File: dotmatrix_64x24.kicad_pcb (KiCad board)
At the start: 2 copper layers, 180 x 100 mm, 788 parts, among them CON1 BARREL_JACK, P1 CONN_01X09, P2 CONN_01X09, P3 CONN_01X04, P4 CONN_01X03, P5 USB_OTG, P6 CONN_01X03, Q1 NJL7302L-F3, Q3 Q_NPN_BCE RN5006, SW1 SW_PUSH_SMALL_H, SW2 SW_PUSH_SMALL_H, SW3 SW_PUSH_SMALL_H, SW4 SW_PUSH_SMALL_H, SW5 SW_PUSH_SMALL_H, SW6 SW_PUSH_SMALL_H, SW7 SW_PUSH_SMALL_H, SW8 SW_PUSH_SMALL_H, U1 WROOM-02, U10 LED1642GW, U11 LED1642GW, U12 AE-BME280, U13 TPS54426, U14 NJU7223, U15 DS1307, U16 CH340G, U17 OSRB38C9AA, U18 BME280, U2 74HC595-alt-vdd, U3 TD62783, U4 74HC595-alt-vdd, U5 TD62783, U6 LED1642GW, U7 74HC595-alt-vdd, U8 TD62783, U9 LED1642GW, X1 CRYSTAL_SMD, Y1 12MHz

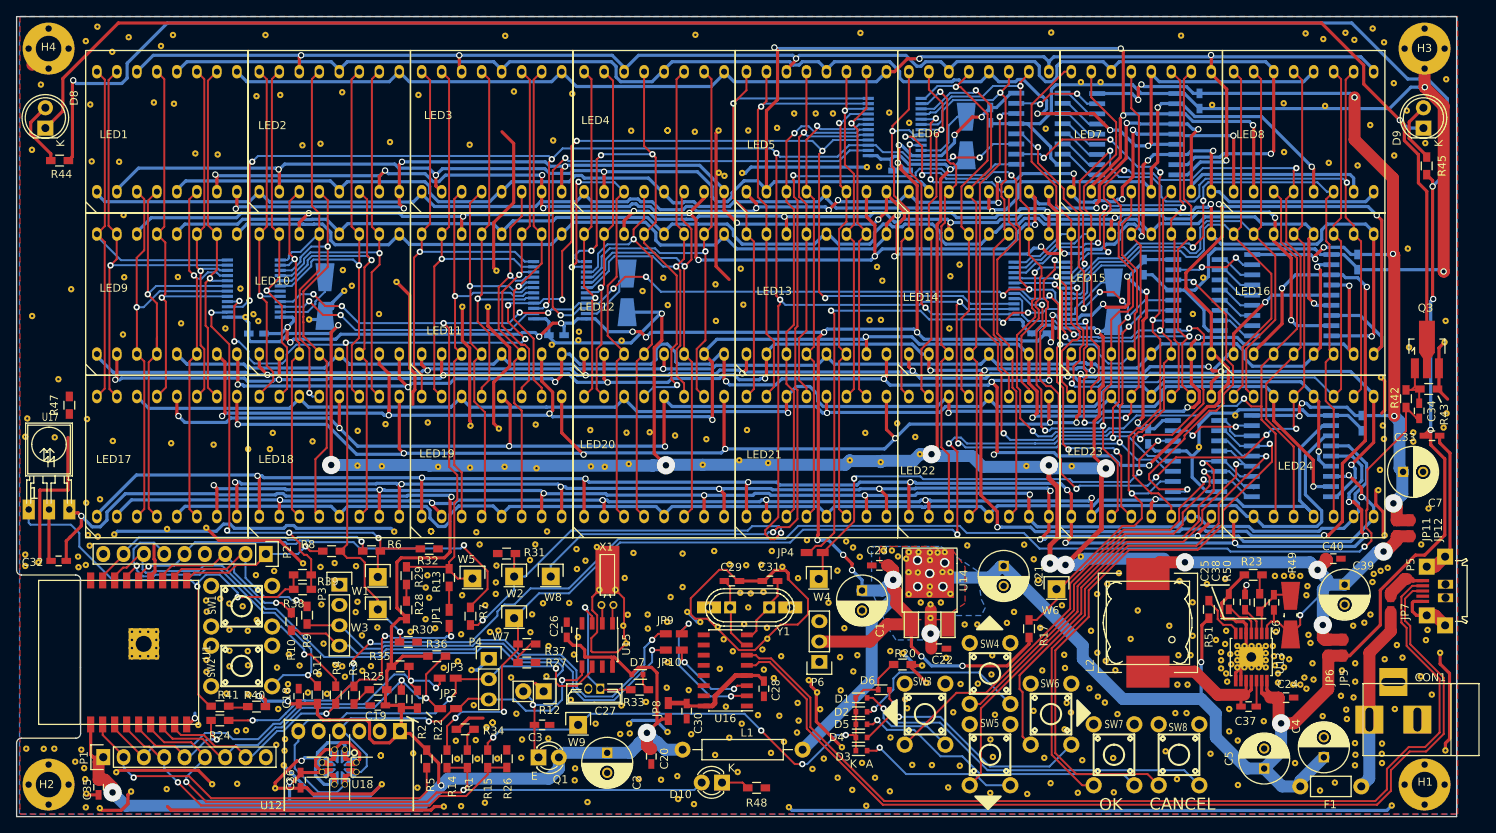
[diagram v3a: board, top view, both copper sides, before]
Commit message: Trace fixes
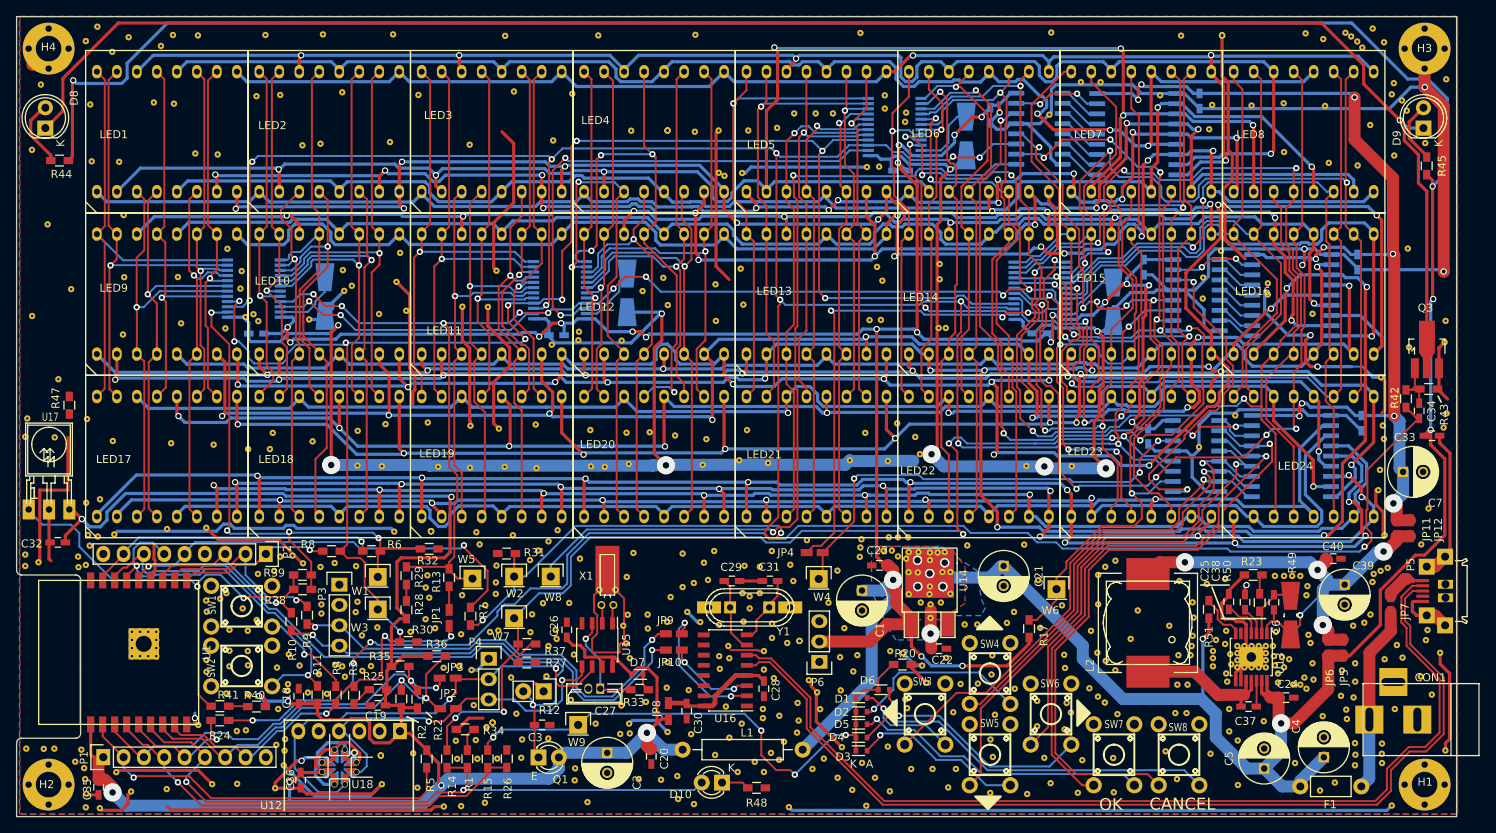
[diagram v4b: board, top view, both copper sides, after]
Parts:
- removed the REF** at (105.8, 88.4)
- removed the REF** at (99.6, 88.3)
- removed the REF** at (107.7, 80.8)
- removed the REF** at (101.1, 80.5)
- removed the REF** at (109.7, 82.2)
- removed the REF** at (139.1, 79.8)
- removed the REF** at (82.2, 89.6)
- removed the REF** at (103.5, 85.9)
- removed the REF** at (105.8, 89.8)
- removed the REF** at (105.1, 80.5)
- removed the REF** at (50.4, 90.4)
- removed the REF** at (159.0, 49.2)
- removed the REF** at (120.0, 67.7)
- removed the REF** at (83.1, 80.0)
- removed the REF** at (84.5, 78.3)
- removed the REF** at (82.0, 81.1)
- removed the REF** at (121.2, 102.1)
- removed the REF** at (186.6, 64.0)
- removed the REF** at (186.6, 65.1)
- removed the REF** at (140.6, 26.0)
- removed the REF** at (102.9, 87.9)
- removed the REF** at (105.2, 91.1)
- removed the REF** at (101.5, 91.3)
- removed the REF** at (103.2, 80.6)
- removed the REF** at (103.8, 84.1)
- removed the REF** at (102.5, 84.0)
- removed the REF** at (105.4, 83.9)
- removed the REF** at (100.4, 89.8)
- removed the REF** at (82.0, 78.6)
- removed the REF** at (67.2, 92.6)
- removed the REF** at (145.0, 79.5)
- added REF**: stitch-via-0.6mm, components:stitch-via-0.8mm, F.Cu at (161.1, 26.1)
- added REF**: stitch-via-0.6mm, components:stitch-via-0.8mm, F.Cu at (179.6, 15.1)
- added REF**: stitch-via-0.6mm, components:stitch-via-0.8mm, F.Cu at (185.2, 22.5)
- added REF**: stitch-via-0.6mm, components:stitch-via-0.8mm, F.Cu at (183.9, 21.7)
- added REF** (x2): stitch-via-0.6mm, components:stitch-via-0.8mm, F.Cu at (109.9, 90.0)
- added REF**: stitch-via-0.6mm, components:stitch-via-0.8mm, F.Cu at (59.9, 41.5)
- added REF**: stitch-via-0.6mm, components:stitch-via-0.8mm, F.Cu at (60.7, 48.8)
- added REF**: stitch-via-0.6mm, components:stitch-via-0.8mm, F.Cu at (38.4, 41.0)
- added REF**: stitch-via-0.6mm, components:stitch-via-0.8mm, F.Cu at (40.1, 43.8)
- added REF**: stitch-via-0.6mm, components:stitch-via-0.8mm, F.Cu at (123.2, 24.0)
- added REF**: stitch-via-0.6mm, components:stitch-via-0.8mm, F.Cu at (141.1, 24.3)
- added REF**: stitch-via-0.6mm, components:stitch-via-0.8mm, F.Cu at (120.5, 21.8)
- added REF**: stitch-via-0.6mm, components:stitch-via-0.8mm, F.Cu at (127.3, 50.9)
- added REF**: stitch-via-0.6mm, components:stitch-via-0.8mm, F.Cu at (174.0, 49.1)
- added REF**: stitch-via-0.6mm, components:stitch-via-0.8mm, F.Cu at (168.4, 46.7)
- added REF**: stitch-via-0.6mm, components:stitch-via-0.8mm, F.Cu at (168.4, 45.3)
- added REF**: stitch-via-0.6mm, components:stitch-via-0.8mm, F.Cu at (160.3, 47.2)
- added REF**: stitch-via-0.6mm, components:stitch-via-0.8mm, F.Cu at (162.6, 41.3)
- added REF** (x2): stitch-via-0.6mm, components:stitch-via-0.8mm, F.Cu at (162.7, 14.4)
- added REF**: stitch-via-0.6mm, components:stitch-via-0.8mm, F.Cu at (154.9, 21.8)
- added REF**: stitch-via-0.6mm, components:stitch-via-0.8mm, F.Cu at (166.4, 23.1)
- added REF**: stitch-via-0.6mm, components:stitch-via-0.8mm, F.Cu at (103.6, 84.5)
- added REF**: stitch-via-0.6mm, components:stitch-via-0.8mm, F.Cu at (102.9, 87.6)
- added REF**: stitch-via-0.6mm, components:stitch-via-0.8mm, F.Cu at (108.7, 80.5)
- added REF**: stitch-via-0.6mm, components:stitch-via-0.8mm, F.Cu at (97.9, 80.3)
- added REF**: stitch-via-0.6mm, components:stitch-via-0.8mm, F.Cu at (96.6, 82.8)
- added REF**: stitch-via-0.6mm, components:stitch-via-0.8mm, F.Cu at (99.8, 91.9)
- added REF**: stitch-via-0.6mm, components:stitch-via-0.8mm, F.Cu at (108.3, 90.3)
- added REF**: stitch-via-0.6mm, components:stitch-via-0.8mm, F.Cu at (98.4, 82.4)
- added REF**: stitch-via-0.6mm, components:stitch-via-0.8mm, F.Cu at (109.1, 82.5)
- added REF**: stitch-via-0.6mm, components:stitch-via-0.8mm, F.Cu at (103.0, 80.6)
- added REF**: stitch-via-0.6mm, components:stitch-via-0.8mm, F.Cu at (15.9, 38.0)
- added REF**: stitch-via-0.6mm, components:stitch-via-0.8mm, F.Cu at (104.9, 80.8)
- added REF**: stitch-via-0.6mm, components:stitch-via-0.8mm, F.Cu at (104.9, 84.1)
- added REF**: stitch-via-0.6mm, components:stitch-via-0.8mm, F.Cu at (105.3, 99.7)
- added REF**: stitch-via-0.6mm, components:stitch-via-0.8mm, F.Cu at (101.1, 92.2)
- added REF**: stitch-via-0.6mm, components:stitch-via-0.8mm, F.Cu at (101.0, 90.7)
- added REF**: stitch-via-0.6mm, components:stitch-via-0.8mm, F.Cu at (106.4, 89.7)
- added REF**: stitch-via-0.6mm, components:stitch-via-0.8mm, F.Cu at (106.4, 87.9)
- added REF**: stitch-via-0.6mm, components:stitch-via-0.8mm, F.Cu at (102.7, 84.1)
- added REF**: stitch-via-0.6mm, components:stitch-via-0.8mm, F.Cu at (103.6, 86.0)
- added REF**: stitch-via-0.6mm, components:stitch-via-0.8mm, F.Cu at (99.8, 88.0)
- added REF**: stitch-via-0.6mm, components:stitch-via-0.8mm, F.Cu at (34.7, 14.4)
- added REF**: stitch-via-0.6mm, components:stitch-via-0.8mm, F.Cu at (159.1, 87.1)
- added REF**: stitch-via-0.6mm, components:stitch-via-0.8mm, F.Cu at (158.9, 90.7)
- added REF**: stitch-via-0.6mm, components:stitch-via-0.8mm, F.Cu at (139.6, 97.5)
- added REF**: stitch-via-0.6mm, components:stitch-via-0.8mm, F.Cu at (147.2, 85.5)
- added REF**: stitch-via-0.6mm, components:stitch-via-0.8mm, F.Cu at (120.9, 103.3)
- added REF**: stitch-via-0.6mm, components:stitch-via-0.8mm, F.Cu at (120.9, 67.6)
- added REF**: stitch-via-0.6mm, components:stitch-via-0.8mm, F.Cu at (123.4, 77.1)
- added REF**: stitch-via-0.6mm, components:stitch-via-0.8mm, F.Cu at (122.2, 77.1)
- added REF**: stitch-via-0.6mm, components:stitch-via-0.8mm, F.Cu at (121.0, 77.1)
- added REF**: stitch-via-0.6mm, components:stitch-via-0.8mm, F.Cu at (105.4, 106.4)
- added REF**: stitch-via-0.6mm, components:stitch-via-0.8mm, F.Cu at (50.3, 14.2)
- added REF**: stitch-via-0.6mm, components:stitch-via-0.8mm, F.Cu at (104.3, 105.2)
- added REF**: stitch-via-0.6mm, components:stitch-via-0.8mm, F.Cu at (107.3, 104.9)
- added REF**: stitch-via-0.6mm, components:stitch-via-0.8mm, F.Cu at (46.5, 79.4)
- added REF**: stitch-via-0.6mm, components:stitch-via-0.8mm, F.Cu at (45.0, 79.5)
- added REF**: stitch-via-0.6mm, components:stitch-via-0.8mm, F.Cu at (82.4, 79.8)
- added REF**: stitch-via-0.6mm, components:stitch-via-0.8mm, F.Cu at (67.3, 93.2)
- added REF**: stitch-via-0.6mm, components:stitch-via-0.8mm, F.Cu at (74.0, 76.8)
- added REF**: stitch-via-0.6mm, components:stitch-via-0.8mm, F.Cu at (77.2, 78.7)
- added REF**: stitch-via-0.6mm, components:stitch-via-0.8mm, F.Cu at (88.6, 92.2)
- added REF**: stitch-via-0.6mm, components:stitch-via-0.8mm, F.Cu at (79.5, 89.8)
- added REF**: stitch-via-0.6mm, components:stitch-via-0.8mm, F.Cu at (59.1, 14.2)
- added REF**: stitch-via-0.6mm, components:stitch-via-0.8mm, F.Cu at (79.4, 88.6)
- added REF**: stitch-via-0.6mm, components:stitch-via-0.8mm, F.Cu at (50.1, 86.6)
- added REF**: stitch-via-0.6mm, components:stitch-via-0.8mm, F.Cu at (84.7, 14.4)
- added REF**: stitch-via-0.6mm, components:stitch-via-0.8mm, F.Cu at (180.2, 15.9)
- moved REF** 4.12 mm to (136.8, 96.0)
- moved REF** 2.49 mm to (127.4, 42.9)
- moved REF** 2.39 mm to (147.2, 81.8)
- moved C32 2.31 mm to (17.1, 77.7)
- moved REF** 2.25 mm to (105.4, 91.3)
- moved REF** 2.17 mm to (148.1, 80.8)
- moved REF** 1.98 mm to (139.6, 100.7)
- moved REF** 1.92 mm to (117.6, 77.3)
- moved REF** 1.69 mm to (78.5, 77.6)
- moved REF** 1.61 mm to (149.4, 80.0)
- moved REF** 1.40 mm to (127.4, 44.8)
- moved REF** 1.34 mm to (38.2, 84.1)
- moved REF** 1.33 mm to (79.6, 76.2)
- moved REF** 1.05 mm to (161.5, 92.2)
- moved REF** 1.05 mm to (161.5, 93.2)
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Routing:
- net GND: track 1068.8 -> 1059.9 mm, vias 16 -> 19
- net /LEDLOGICVDD: track 313.1 -> 306.8 mm, vias 24 -> 21
- net /ESPVDD: track 289.0 -> 283.2 mm
- net /Sheet57A04605/HC595LATCH: track 183.5 -> 188.7 mm, vias 10 -> 11
- net Net-(C27-Pad1): track 17.2 -> 13.1 mm
- net /Sheet57A04605/r2: track 181.9 -> 185.4 mm
- net /Sheet57A04605/BUTTONSENSE: track 66.6 -> 69.4 mm
- net /IR_OUT: track 178.7 -> 180.8 mm
- net /Sheet57A04605/r9: track 182.0 -> 184.0 mm
- net /Sheet57A04605/HC595SER: track 59.8 -> 57.9 mm
- net Net-(D3-Pad2): track 20.0 -> 21.7 mm
- net /Sheet57A04605/SEL6: track 76.8 -> 78.3 mm
- net /Sheet57A04605/SEL5: track 66.9 -> 68.4 mm
- net /Sheet57A04605/SEL1: track 61.1 -> 62.6 mm
- net /Sheet57A04605/SEL2: track 53.2 -> 54.3 mm
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
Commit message: Improved crystal stability by adding local ground plane
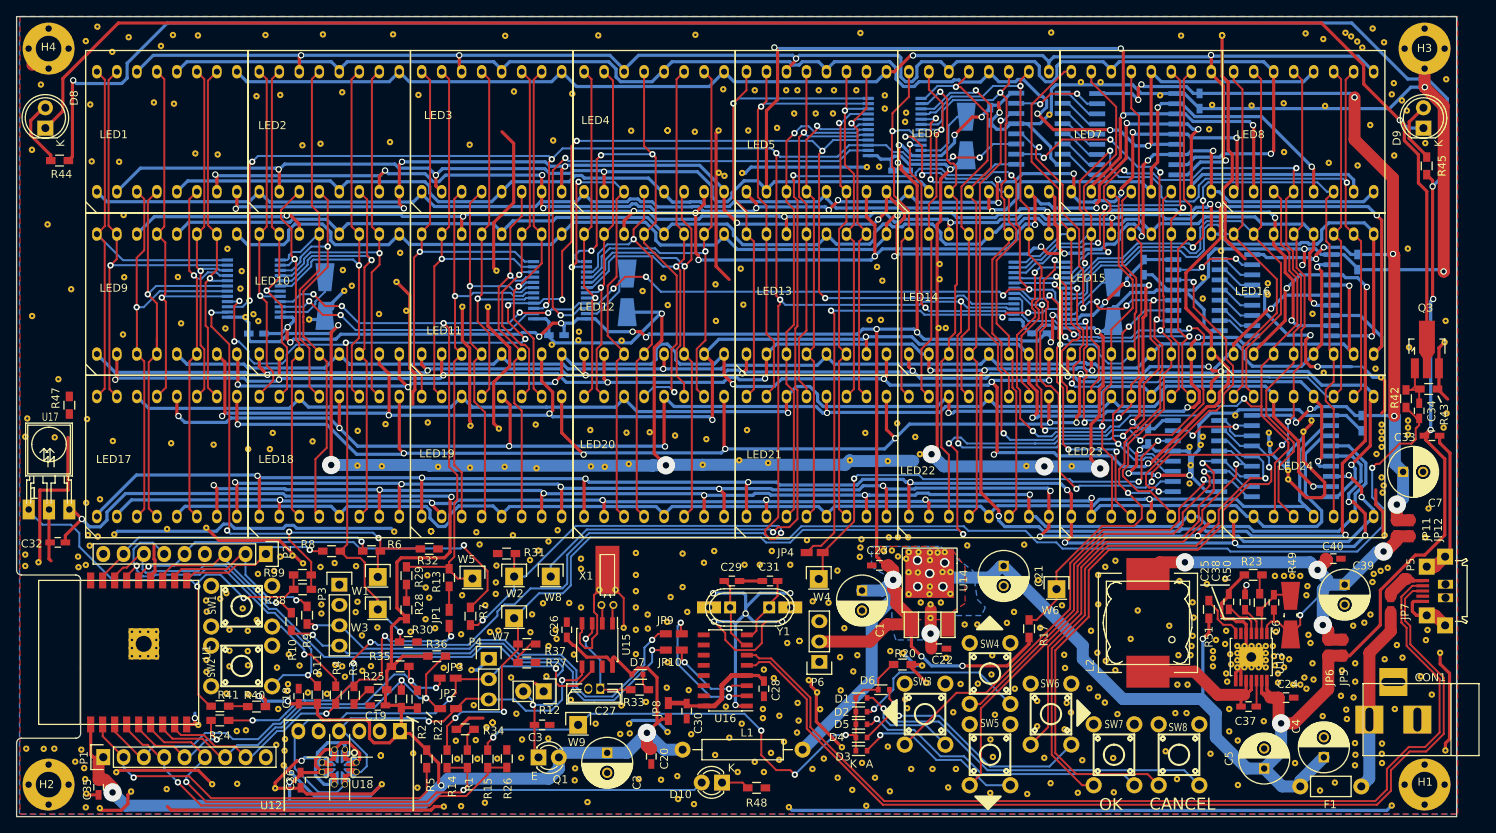
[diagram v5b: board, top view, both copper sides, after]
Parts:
- removed the REF** at (88.3, 82.0)
- removed the REF** at (103.6, 84.5)
- removed the REF** at (88.4, 86.8)
- removed the REF** at (102.9, 87.6)
- removed the REF** at (96.6, 82.8)
- removed the REF** at (99.8, 91.9)
- removed the REF** at (99.9, 93.5)
- removed the REF** at (98.4, 82.4)
- removed the REF** at (88.2, 90.3)
- removed the REF** at (109.1, 82.5)
- removed the REF** at (104.9, 84.1)
- removed the REF** at (101.1, 92.2)
- removed the REF** at (101.0, 90.7)
- removed the REF** at (106.4, 89.7)
- removed the REF** at (106.4, 87.9)
- removed the REF** at (102.7, 84.1)
- removed the REF** at (103.6, 86.0)
- removed the REF** at (99.8, 88.0)
- removed the REF** at (87.8, 88.1)
- removed the REF** at (182.4, 68.7)
- removed the REF** at (105.4, 91.3)
- removed the REF** at (97.5, 87.7)
- added REF**: stitch-via-0.6mm, components:stitch-via-0.8mm, F.Cu at (111.5, 85.1)
- added REF**: stitch-via-0.6mm, components:stitch-via-0.8mm, F.Cu at (104.3, 21.2)
- added REF**: stitch-via-0.6mm, components:stitch-via-0.8mm, F.Cu at (108.2, 21.2)
- added REF**: stitch-via-0.6mm, components:stitch-via-0.8mm, F.Cu at (109.6, 21.2)
- added REF**: stitch-via-0.6mm, components:stitch-via-0.8mm, F.Cu at (112.3, 21.2)
- added REF**: stitch-via-0.6mm, components:stitch-via-0.8mm, F.Cu at (114.2, 21.2)
- added REF**: stitch-via-0.6mm, components:stitch-via-0.8mm, F.Cu at (117.0, 21.2)
- added REF**: stitch-via-0.6mm, components:stitch-via-0.8mm, F.Cu at (158.6, 70.4)
- added REF**: stitch-via-0.6mm, components:stitch-via-0.8mm, F.Cu at (158.8, 68.1)
- added REF**: stitch-via-0.6mm, components:stitch-via-0.8mm, F.Cu at (160.0, 65.5)
- added REF**: stitch-via-0.6mm, components:stitch-via-0.8mm, F.Cu at (181.9, 56.0)
- added REF**: stitch-via-0.6mm, components:stitch-via-0.8mm, F.Cu at (82.5, 85.9)
- added REF**: stitch-via-0.6mm, components:stitch-via-0.8mm, F.Cu at (182.6, 64.8)
- added REF**: stitch-via-0.6mm, components:stitch-via-0.8mm, F.Cu at (182.6, 63.9)
- added REF**: stitch-via-0.6mm, components:stitch-via-0.8mm, F.Cu at (185.9, 64.3)
- added REF**: stitch-via-0.6mm, components:stitch-via-0.8mm, F.Cu at (182.0, 66.7)
- added REF**: stitch-via-0.6mm, components:stitch-via-0.8mm, F.Cu at (185.9, 63.4)
- added REF**: stitch-via-0.6mm, components:stitch-via-0.8mm, F.Cu at (185.9, 62.5)
- added REF**: stitch-via-0.6mm, components:stitch-via-0.8mm, F.Cu at (182.9, 70.6)
- added REF**: stitch-via-0.6mm, components:stitch-via-0.8mm, F.Cu at (182.6, 69.6)
- added REF**: stitch-via-0.6mm, components:stitch-via-0.8mm, F.Cu at (175.4, 56.5)
- added REF**: stitch-via-0.6mm, components:stitch-via-0.8mm, F.Cu at (170.9, 69.8)
- added REF**: stitch-via-0.6mm, components:stitch-via-0.8mm, F.Cu at (82.5, 81.0)
- added REF**: stitch-via-0.6mm, components:stitch-via-0.8mm, F.Cu at (170.9, 68.7)
- added REF**: stitch-via-0.6mm, components:stitch-via-0.8mm, F.Cu at (172.8, 63.9)
- added REF**: stitch-via-0.6mm, components:stitch-via-0.8mm, F.Cu at (173.9, 62.5)
- added REF**: stitch-via-0.6mm, components:stitch-via-0.8mm, F.Cu at (160.3, 64.5)
- added REF**: stitch-via-0.6mm, components:stitch-via-0.8mm, F.Cu at (168.7, 65.4)
- added REF**: stitch-via-0.6mm, components:stitch-via-0.8mm, F.Cu at (168.5, 64.0)
- added REF**: stitch-via-0.6mm, components:stitch-via-0.8mm, F.Cu at (89.4, 81.8)
- added REF**: stitch-via-0.6mm, components:stitch-via-0.8mm, F.Cu at (89.4, 83.8)
- added REF**: stitch-via-0.6mm, components:stitch-via-0.8mm, F.Cu at (89.4, 85.9)
- added REF**: stitch-via-0.6mm, components:stitch-via-0.8mm, F.Cu at (89.4, 88.6)
- added REF**: stitch-via-0.6mm, components:stitch-via-0.8mm, F.Cu at (87.9, 88.4)
- added REF**: stitch-via-0.6mm, components:stitch-via-0.8mm, F.Cu at (100.3, 21.1)
- moved REF** 1.18 mm to (158.6, 65.8)
- moved REF** 1.03 mm to (182.6, 65.8)
- moved REF** 1.02 mm to (188.1, 77.1)
- moved REF** 0.92 mm to (89.4, 91.7)
- moved REF** 0.61 mm to (182.8, 71.5)
- moved REF** 0.30 mm to (89.4, 79.0)
- moved REF** 0.25 mm to (104.9, 80.5)
- moved REF** 0.20 mm to (182.6, 63.0)
- moved REF** 0.13 mm to (103.0, 80.5)
- moved REF** 0.13 mm to (82.5, 79.8)
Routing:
- net GND: track 1059.9 -> 1142.7 mm, vias 19 -> 29
- net Net-(U4-Pad14): track 41.5 -> 38.8 mm
- net /Sheet57A04605/HC595RESET: track 96.3 -> 98.0 mm
- net /Sheet57A04605/c53: track 71.1 -> 72.7 mm
- net /Sheet57A04605/c59: track 90.3 -> 91.6 mm
- net /Sheet57A04605/c58: track 102.0 -> 103.3 mm
- net /IR_OUT: track 180.8 -> 182.2 mm
- net /Sheet57A04605/r15: track 262.0 -> 263.0 mm
- net /Sheet57A04605/HC595LATCH: track 188.7 -> 189.6 mm, vias 11 -> 10
- net /ESPVDD: track 283.2 -> 282.3 mm
- net /Sheet57A04605/c50: track 72.6 -> 71.8 mm
- net /Sheet57A04605/r20: track 181.9 -> 182.7 mm
- net /Sheet57A04605/c57: track 111.0 -> 111.7 mm
- net /Sheet57A04605/HC595SER: track 57.9 -> 58.5 mm
- net /Sheet57A04605/LEDVDD: track 131.6 -> 131.1 mm
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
